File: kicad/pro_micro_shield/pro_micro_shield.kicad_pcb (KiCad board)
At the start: 2 copper layers, 42 x 41 mm, 14 parts, among them U0 ProMicro

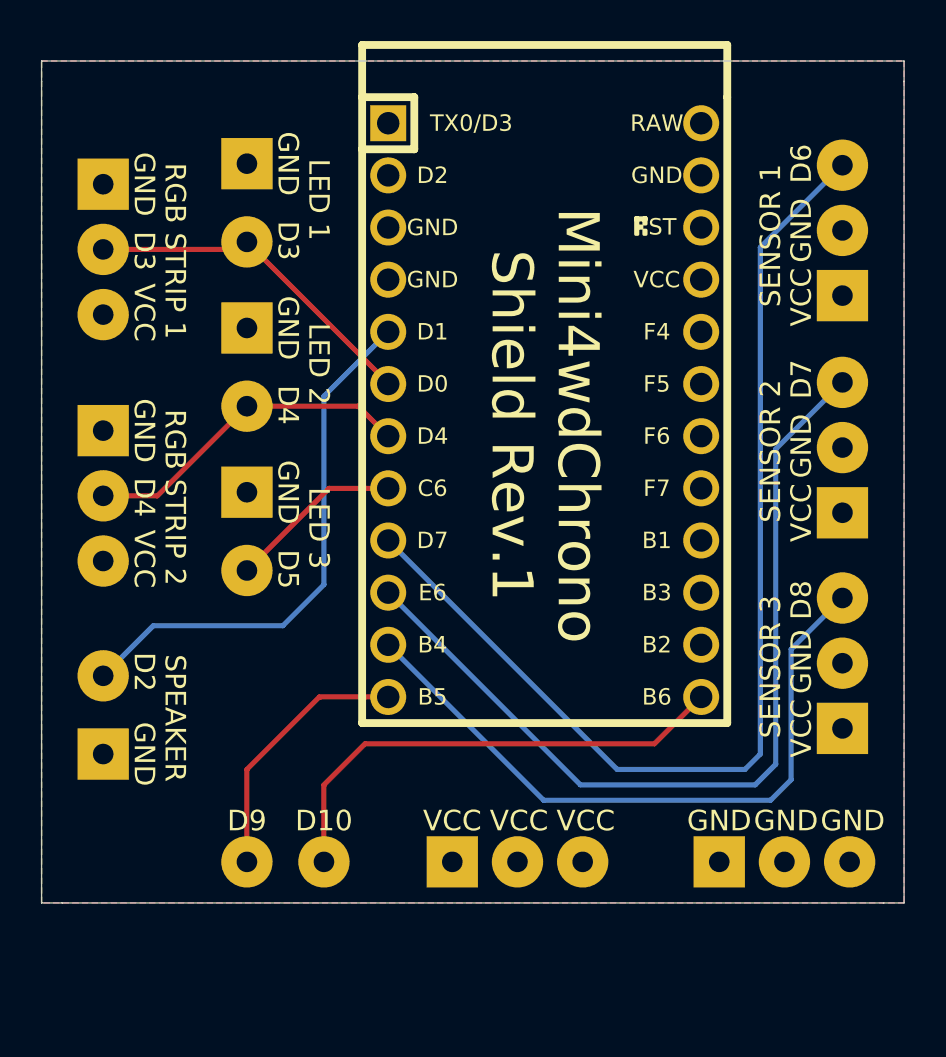
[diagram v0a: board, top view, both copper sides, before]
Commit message: cleanup shield kicad project and readme
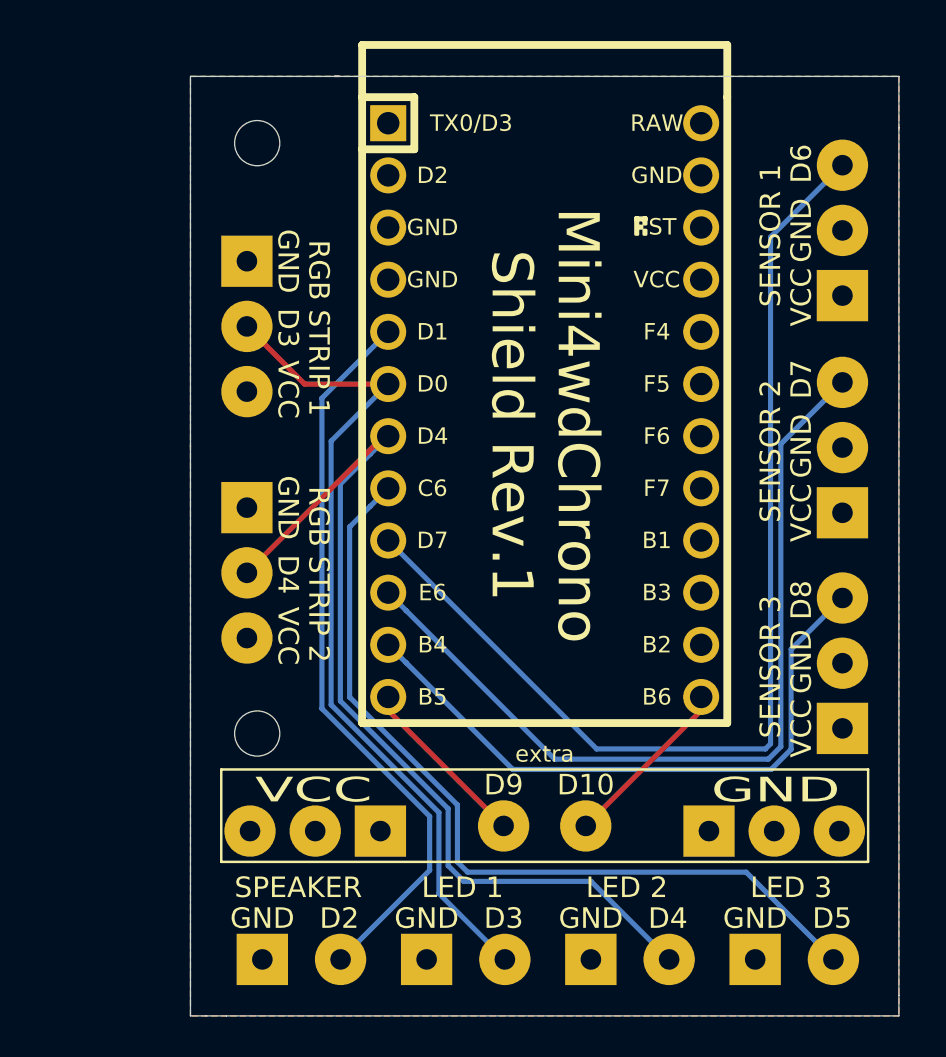
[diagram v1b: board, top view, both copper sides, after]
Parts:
- added H0: MountingHole, MountingHole:MountingHole_2.2mm_M2, F.Cu at (160.5, 74.0)
- added H1: MountingHole, MountingHole:MountingHole_2.2mm_M2, F.Cu at (160.5, 102.8)
- moved JL0 39.7 mm to (168.8, 113.8), turned to 0 degrees
- moved JL1 35.0 mm to (176.8, 113.8), turned to 0 degrees
- moved JL2 33.6 mm to (184.8, 113.8), turned to 0 degrees
- moved JPIN1 12.9 mm to (176.5, 107.2)
- moved JSPEAKER0 12.7 mm to (160.8, 113.8), turned to 0 degrees
- moved JPIN0 12.6 mm to (172.5, 107.2)
- moved JRGB0 7.94 mm to (160.0, 79.8)
- moved JRGB1 7.94 mm to (160.0, 91.8)
- moved JVCC0 3.81 mm to (166.5, 107.5), turned to 180 degrees
- moved JGND0 1.58 mm to (182.5, 107.5)
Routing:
- net Net-(JL2-Pad2): track 8.54 -> 41.4 mm
- net Net-(JL1-Pad2): track 16.3 -> 46.3 mm
- net Net-(JL0-Pad2): track 16.9 -> 40.7 mm
- net Net-(JPIN1-Pad1): track 23.9 -> 8.61 mm
- net Net-(JSPEAKER0-Pad2): track 26.2 -> 35.9 mm
- net Net-(JPIN0-Pad1): track 12.8 -> 8.61 mm
- net Net-(JS2-Pad3): track 33.1 -> 30.9 mm
- net Net-(JS1-Pad3): track 43.1 -> 41.7 mm
- net Net-(JS0-Pad3): track 53.4 -> 52.6 mm
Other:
- board size 42 x 41 mm -> 34.5 x 45.8 mm
- board text added: "extra"

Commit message: cleanup shield kicad project and readme
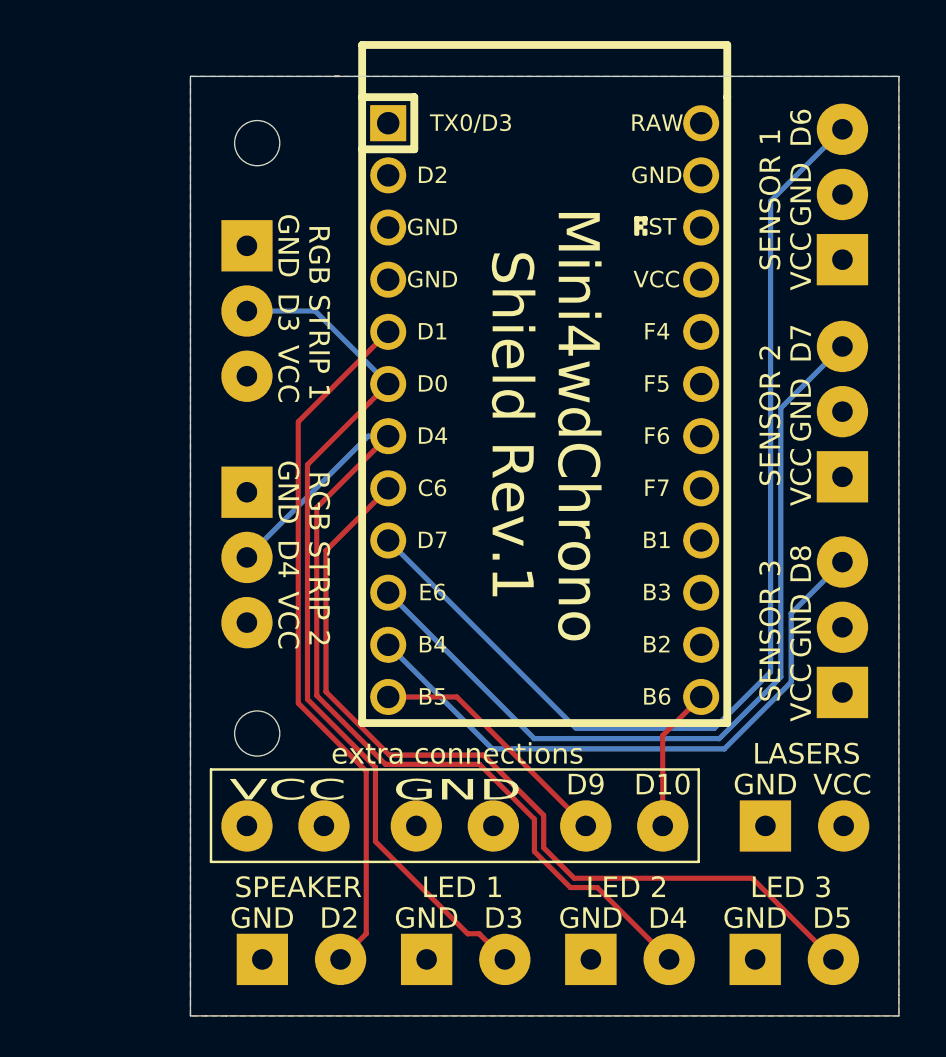
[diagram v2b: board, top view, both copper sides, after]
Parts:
- added JGND1: Conn_01x01_Female, Connector_Wire:SolderWirePad_1x01_Drill1mm, F.Cu at (168.2, 107.2)
- added JLASER0: Conn_01x02_Female, Connector_Wire:SolderWirePad_1x02_P3.81mm_Drill1mm, F.Cu at (185.2, 107.2)
- added JVCC1: Conn_01x01_Female, Connector_Wire:SolderWirePad_1x01_Drill1mm, F.Cu at (163.8, 107.2)
- JGND0, JVCC0: value Conn_01x03_Female -> Conn_01x01_Female; footprint Connector_Wire:SolderWirePad_1x03_P3.175mm_Drill1mm -> Connector_Wire:SolderWirePad_1x01_Drill1mm
- moved JGND0 10.5 mm to (172.0, 107.2)
- moved JVCC0 6.50 mm to (160.0, 107.2), turned to 0 degrees
- moved JPIN0 4.00 mm to (176.5, 107.2)
- moved JPIN1 3.75 mm to (180.2, 107.2)
- moved JS0 1.75 mm to (189.0, 79.7)
- moved JS1 1.75 mm to (189.0, 90.2)
- moved JS2 1.75 mm to (189.0, 100.8)
- moved JRGB0 0.75 mm to (160.0, 79.0)
- moved JRGB1 0.75 mm to (160.0, 91.0)
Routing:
- net Net-(JPIN0-Pad1): track 8.61 -> 12.9 mm
- net Net-(JSPEAKER0-Pad2): track 35.9 -> 34.3 mm
- net Net-(JL0-Pad2): track 40.7 -> 42.3 mm
- net Net-(JS0-Pad3): track 52.6 -> 51.4 mm
- net Net-(JS1-Pad3): track 41.7 -> 40.7 mm
- net Net-(JS2-Pad3): track 30.9 -> 30.0 mm
- net Net-(JPIN1-Pad1): track 8.61 -> 7.71 mm
- net Net-(JL2-Pad2): track 41.4 -> 42.2 mm
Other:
- board text added: "LASERS"
- board text added: "extra connections"
- board text removed: "extra"
